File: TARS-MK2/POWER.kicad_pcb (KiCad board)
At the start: 2 copper layers, 69.9 x 162.4 mm, 26 parts, among them J1 505578-0671, J2 505567-0871, J3 505567-0871, J4 505578-0671, J5 505567-0871, J6 505567-0871, J7 Conn_02x03_Top_Bottom_Mountin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, J701 XT60, J702 XT60, J706 XT60, J8 Conn_02x03_Top_Bottom_Mountin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, U701 D36V28F3, U702 D24V50F5, U703 LM7809_TO220, U704 D36V50F6, U705 D36V50F6, U706 D36V50F6, U707 D36V50F6

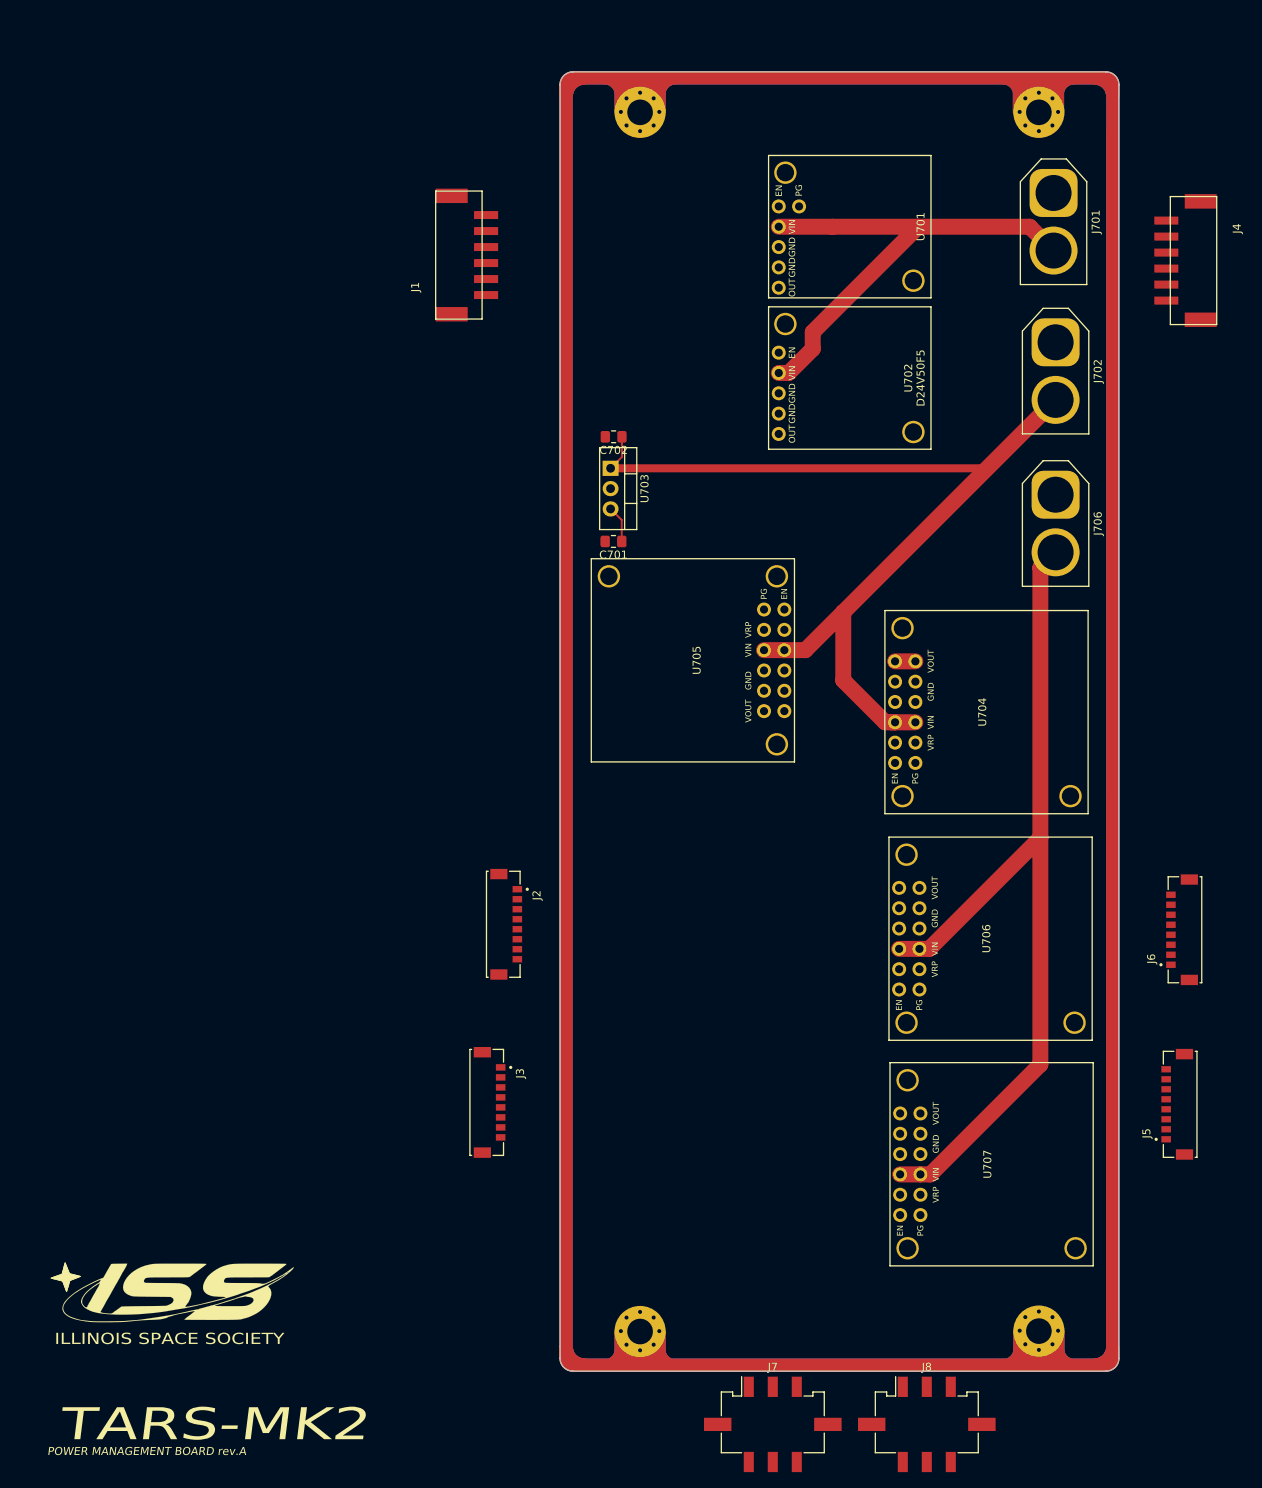
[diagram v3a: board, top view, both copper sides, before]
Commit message: Routed Power Board
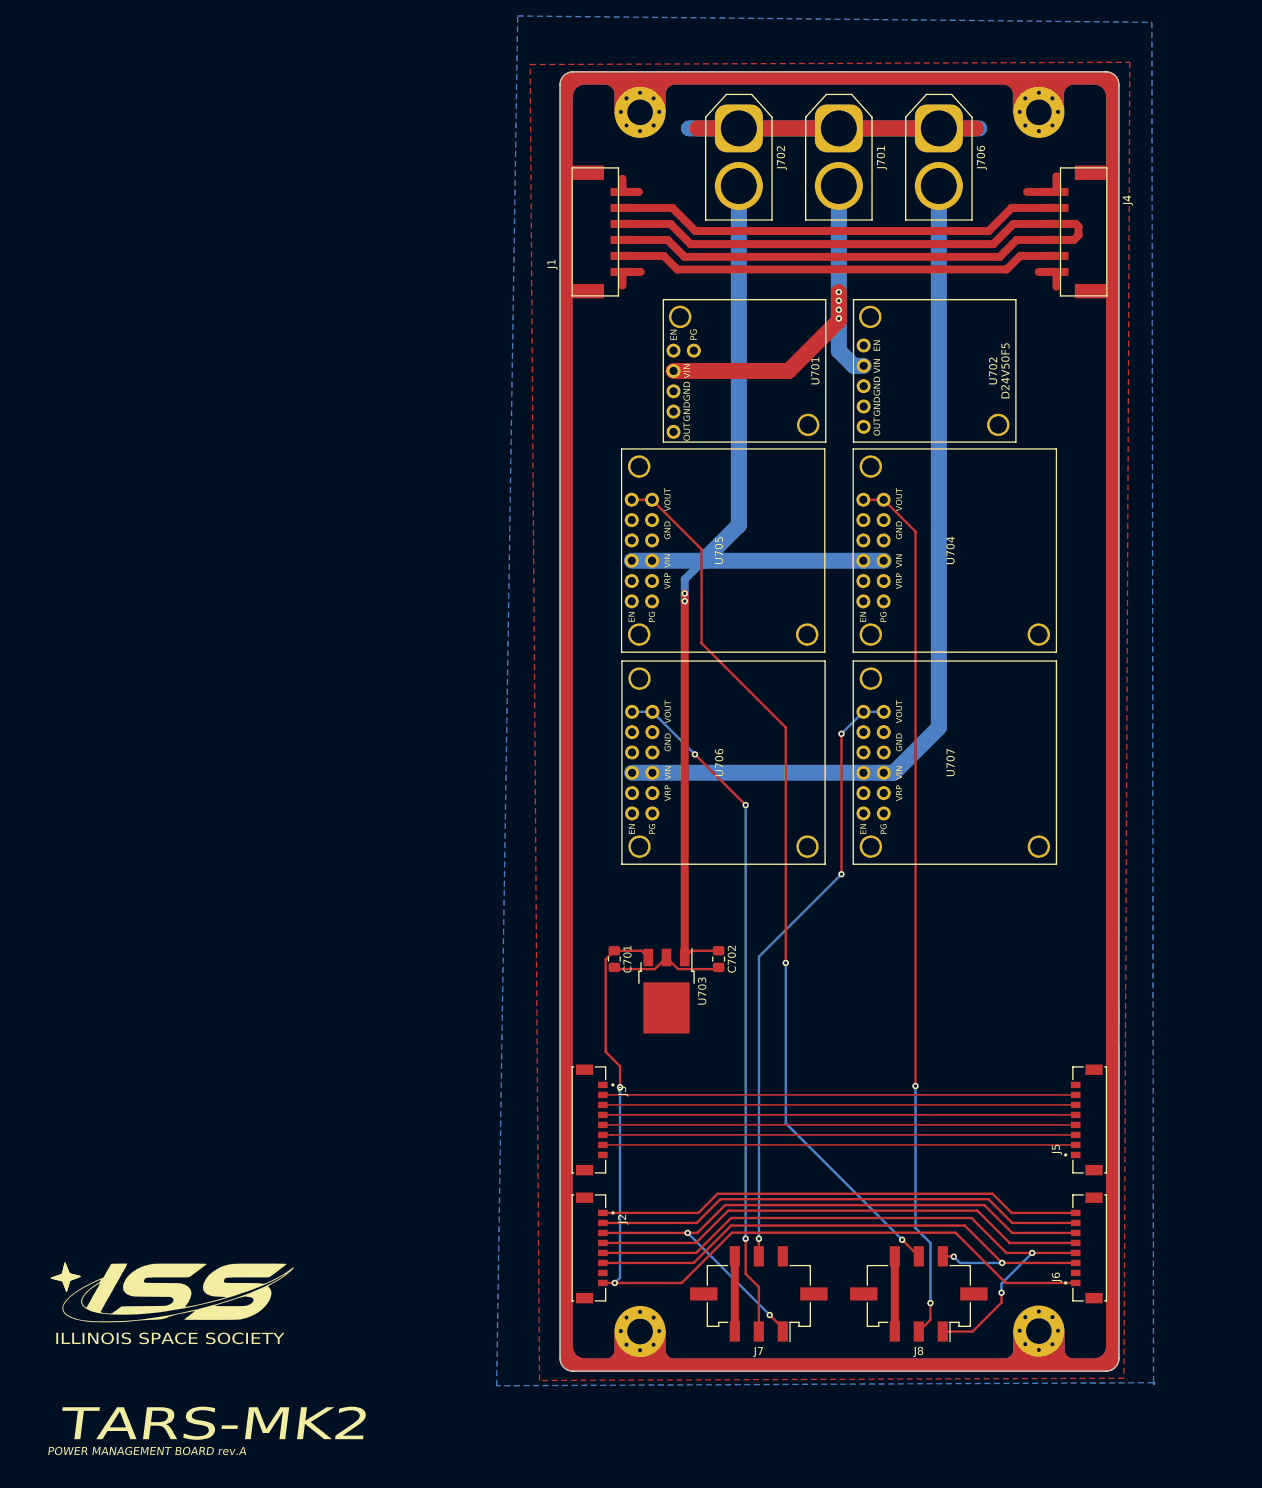
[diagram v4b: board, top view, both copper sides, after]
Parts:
- U703: footprint Package_TO_SOT_THT:TO-220-3_Vertical -> Package_TO_SOT_SMD:TO-252-3_TabPin2
- moved C702 66.6 mm to (201.7, 170.7), turned to 270 degrees
- moved U703 65.7 mm to (195.2, 174.7)
- moved C701 52.2 mm to (188.7, 170.7), turned to 270 degrees
- moved U707 50.4 mm to (218.6, 133.4)
- moved J706 48.1 mm to (229.2, 66.9)
- moved J702 47.8 mm to (204.2, 66.9)
- moved U705 44.7 mm to (189.6, 106.9), turned to 270 degrees
- moved J2 41.8 mm to (185.5, 206.8)
- moved J6 41.5 mm to (248.1, 206.8)
- moved U706 40.0 mm to (189.6, 133.4)
- moved J701 28.0 mm to (216.7, 66.9)
- moved U701 22.3 mm to (215.1, 97.2)
- moved U704 20.6 mm to (218.5, 106.9)
- moved J1 17.3 mm to (183.4, 79.8)
- moved J7 16.4 mm to (206.7, 212.6), turned to 180 degrees
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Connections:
- J8 pad 2: 6V_AC_SERVO3 -> 6V_HYBRID_SERVO3
- J8 pad 5: 6V_AC_SERVO4 -> 6V_HYBRID_SERVO4
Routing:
- net GND: track 0.00 -> 121.8 mm
- net 5V: track 0.00 -> 119.3 mm
- net 3V3: track 0.00 -> 112.3 mm
- net 6V_HYBRID_SERVO4: track 0.00 -> 110.9 mm, vias 0 -> 2
- net 9V_PT_SUPPLY: track 4.64 -> 111.9 mm, vias 0 -> 2
- net 6V_HYBRID_SERVO3: track 2.54 -> 109.5 mm, vias 0 -> 2
- net 6V_AC_SERVO1: track 0.00 -> 85.5 mm, vias 0 -> 3
- net B2B_SERVO3: track 0.00 -> 79.3 mm, vias 0 -> 2
- net B2B_SERVO1: track 0.00 -> 79.2 mm, vias 0 -> 2
- net 6V_AC_SERVO2: track 0.00 -> 76.0 mm, vias 0 -> 3
- net B2B_SERVO4: track 0.00 -> 70.7 mm, vias 0 -> 2
- net B2B_SERVO2: track 0.00 -> 62.4 mm
- net Net-(J2-Pad2): track 0.00 -> 61.6 mm
- net Net-(J2-Pad1): track 0.00 -> 61.1 mm
- net Net-(J3-Pad7): track 0.00 -> 59.1 mm
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- added copper zone on B.Cu, net GND
- added copper zone on F.Cu, net GND

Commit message: POWER board completed woo
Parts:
- added D101: LED, LED_SMD:LED_0603_1608Metric, F.Cu at (193.2, 96.8)
- added D102: LED, LED_SMD:LED_0603_1608Metric, F.Cu at (240.4, 96.9)
- added J101: 505575-0271, Molex 2 Circuit 2.00mm:505575-0271, F.Cu at (216.7, 83.5)
- added J102: 505575-0271, Molex 2 Circuit 2.00mm:505575-0271, F.Cu at (204.2, 83.5)
- added J103: 505575-0271, Molex 2 Circuit 2.00mm:505575-0271, F.Cu at (229.3, 83.5)
- added R101: 1k, Resistor_SMD:R_0603_1608Metric, F.Cu at (193.2, 99.8)
- added R102: 1k, Resistor_SMD:R_0603_1608Metric, F.Cu at (240.4, 99.9)
- moved G*** 89.0 mm to (216.7, 180.3)
- moved U701 7.09 mm to (215.1, 104.3)
- moved U702 7.09 mm to (238.9, 104.3)
- moved U706 7.09 mm to (189.7, 140.5)
- moved U707 7.09 mm to (218.6, 140.5)
- moved U704 7.09 mm to (218.6, 114.0)
- moved U705 7.09 mm to (189.6, 114.0)
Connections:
- J7 pad 4: B2B_SERV02 -> B2B_SERVO2
- J701 pad 2: Net-(J701-Pad2) -> Net-(J101-Pad2)
- J702 pad 2: Net-(C702-Pad1) -> Net-(J102-Pad2)
- J706 pad 2: Net-(J706-Pad2) -> Net-(J103-Pad2)
- U701 pad 2: Net-(J701-Pad2) -> Net-(J101-Pad1)
- U701 pad 5: 3V3_MCU_SUPPLY -> 3V3
- U702 pad 2: Net-(J701-Pad2) -> Net-(J101-Pad1)
- U702 pad 5: 5V_MPU_SUPPLY -> 5V
- U706 pad 3: Net-(J706-Pad2) -> Net-(J103-Pad1)
- U706 pad 9: Net-(J706-Pad2) -> Net-(J103-Pad1)
- U707 pad 3: Net-(J706-Pad2) -> Net-(J103-Pad1)
- U707 pad 9: Net-(J706-Pad2) -> Net-(J103-Pad1)
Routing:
- net Net-(J706-Pad2): track 108.4 -> 0.00 mm
- net Net-(J103-Pad1): track 0.00 -> 105.1 mm
- net Net-(J701-Pad2): track 51.3 -> 0.00 mm, vias 4 -> 0
- net 5V: track 119.3 -> 170.5 mm, vias 0 -> 6
- net 3V3: track 112.3 -> 160.8 mm, vias 0 -> 4
- net Net-(J101-Pad1): track 0.00 -> 40.0 mm
- net 6V_HYBRID_SERVO4: track 110.9 -> 144.4 mm, vias 2 -> 3
- net Net-(J103-Pad2): track 0.00 -> 16.3 mm
- net Net-(J101-Pad2): track 0.00 -> 16.2 mm
- net Net-(J102-Pad2): track 0.00 -> 16.1 mm
- net B2B_SERVO2: track 62.4 -> 77.2 mm, vias 0 -> 2
- net GND: track 121.8 -> 108.0 mm
- net Net-(C702-Pad1): track 136.3 -> 131.2 mm, vias 2 -> 6
- net 6V_AC_SERVO2: track 76.0 -> 80.8 mm, vias 3 -> 1
- net B2B_SERVO1: track 79.2 -> 82.6 mm
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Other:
- board text added: "3V3_PWR"
- board text added: "5V_PWR"
- board text added: "ACTIVE CTRL SERVO PWR"
- board text added: "COMPUTATION PWR"
- board text added: "HYBRID BV SERVO PWR"

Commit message: re-generated copper fills + more chungus
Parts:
- added G***: LOGO, karnap:chungus, B.Cu at (209.4, 118.7)

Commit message: TARS-MK2 rev.A complete!
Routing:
- net GND: vias 0 -> 72
